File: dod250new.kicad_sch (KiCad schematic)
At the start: 31 parts, among them J1 Barrel_Jack_Switch, J2 NRJ4HF-1, J3 NRJ4HF, SW1 SW_FSW800_3PDT, U1 TL071

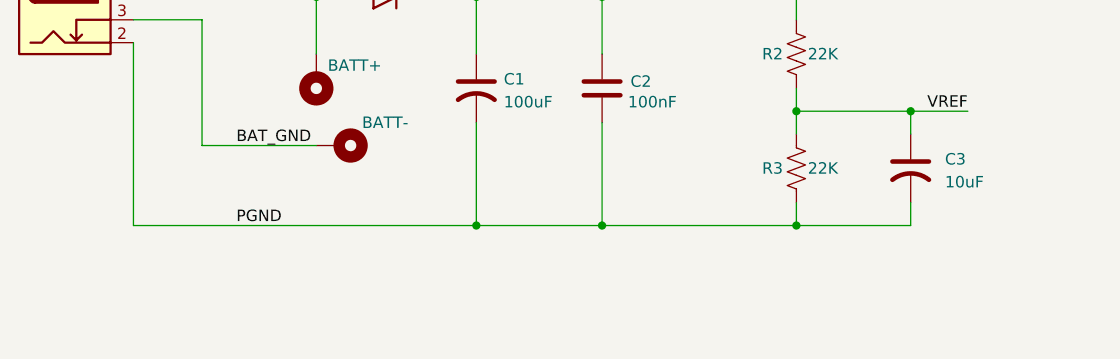
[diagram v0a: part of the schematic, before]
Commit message: v1.2: join AGND and PGND through net tie NT1
AGND (jack sleeves, pot returns, clippers, R1) and PGND (U1 pin 4,
supply filters, DC jack sleeve) were separate nets with no junction
anywhere on the board in v1.0/v1.1 -- no signal return path without
a hand-soldered bond wire. Add Device:NetTie_2 (NT1, copper-only
footprint NetTie:NetTie-2_SMD_Pad0.5mm) as a defined single-point
ground junction, preserving the split-ground netclass intent.
Title block bumped to rev 1.2.

NT1 still needs to be placed and routed in the PCB layout.

Co-Authored-By: Claude Fable 5 <noreply@anthropic.com>
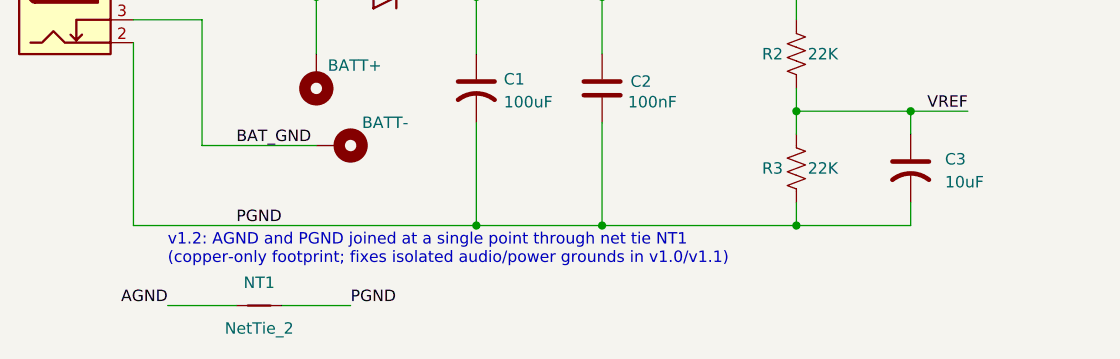
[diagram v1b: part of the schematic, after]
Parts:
- added NT1: NetTie_2, NetTie:NetTie-2_SMD_Pad0.5mm, symbol Device:NetTie_2
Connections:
- net AGND: now also NT1.1
- net PGND: now also NT1.2
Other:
- note added: "v1.2: AGND and PGND joined at a single point through net tie NT1 (copper-only footprint; fixes isolated audio/power grounds in v1.0/v1.1)"
- company: dod250.shupac.com/v1_1 -> dod250.shupac.com/v1_2
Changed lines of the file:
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@@
 	(title_block
 		(title "DOD Overdrive Preamp 250")
-		(date "2026-06-04")
-		(rev "1.1")
-		(company "dod250.shupac.com/v1_1")
+		(date "2026-06-11")
+		(rev "1.2")
+		(company "dod250.shupac.com/v1_2")
 	)
 	(text "(misnomer, it's not LEDA)"
@@
 					(unit 1)
 				)
+			)
+		)
+	)
+	(wire
+		(pts
+			(xy 53.34 193.04) (xy 60.96 193.04)
+		)
+		(stroke
+			(width 0)
+			(type default)
+		)
+	)
+	(wire
+		(pts
+			(xy 66.04 193.04) (xy 73.66 193.04)
+		)
+		(stroke
+			(width 0)
+			(type default)
+		)
+	)
+	(label "AGND"
+		(at 53.34 193.04 180)
+		(effects
+			(font
+				(size 1.27 1.27)
+			)
+			(justify right bottom)
+		)
+	)
+	(label "PGND"
+		(at 73.66 193.04 0)
+		(effects
+			(font
+				(size 1.27 1.27)
+			)
+			(justify left bottom)
+		)
+	)
+	(text "v1.2: AGND and PGND joined at a single point through net tie NT1\n(copper-only footprint; fixes isolated audio/power grounds in v1.0/v1.1)"
+		(exclude_from_sim no)
+		(at 53.34 188.6 0)
+		(effects
+			(font
+				(size 1.27 1.27)
+			)
+			(justify left bottom)
+		)
+	)
+	(symbol
+		(lib_id "Device:NetTie_2")
+		(at 63.5 193.04 0)
+		(unit 1)
+		(body_style 1)
+		(exclude_from_sim no)
+		(in_bom no)
+		(on_board yes)
+		(in_pos_files yes)
+		(dnp no)
+		(property "Reference" "NT1"
+			(at 63.5 190.5 0)
+			(show_name no)
+			(do_not_autoplace no)
+			(effects
+				(font
+					(size 1.27 1.27)
+				)
+			)
+		)
+		(property "Value" "NetTie_2"
+			(at 63.5 195.58 0)
+			(show_name no)
+			(do_not_autoplace no)
+			(effects
+				(font
+					(size 1.27 1.27)
+				)
+			)
+		)
+		(property "Footprint" "NetTie:NetTie-2_SMD_Pad0.5mm"
+			(at 63.5 193.04 0)
+			(hide yes)
+			(show_name no)
+			(do_not_autoplace no)
+			(effects
+				(font
+					(size 1.27 1.27)
+				)
+			)
+		)
+		(property "Datasheet" "~"
+			(at 63.5 193.04 0)
+			(hide yes)
+			(show_name no)
+			(do_not_autoplace no)
+			(effects
+				(font
+					(size 1.27 1.27)
+				)
+			)
+		)
+		(property "Description" "Net tie, 2 pins"
+			(at 63.5 193.04 0)
+			(hide yes)
+			(show_name no)
+			(do_not_autoplace no)
+			(effects
+				(font
+					(size 1.27 1.27)
+				)
+			)
+		)
+		(pin "1"
+		)
+		(pin "2"
+		)
+		(instances
+			(project "dod250new"
+				(path "/65eca179-3106-4a88-bde8-4fcb23cd7118"
+					(reference "NT1")
+					(unit 1)
+				)
